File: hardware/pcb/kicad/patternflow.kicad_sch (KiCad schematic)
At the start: 35 parts, among them J1 Conn_02x08_Odd_Even, J2 Screw_Terminal_01x02, J3 Screw_Terminal_01x02, SW1 RotaryEncoder_Switch, SW2 RotaryEncoder_Switch, SW3 RotaryEncoder_Switch, SW4 RotaryEncoder_Switch, U1 ESP32-S3-DevKit-44pin

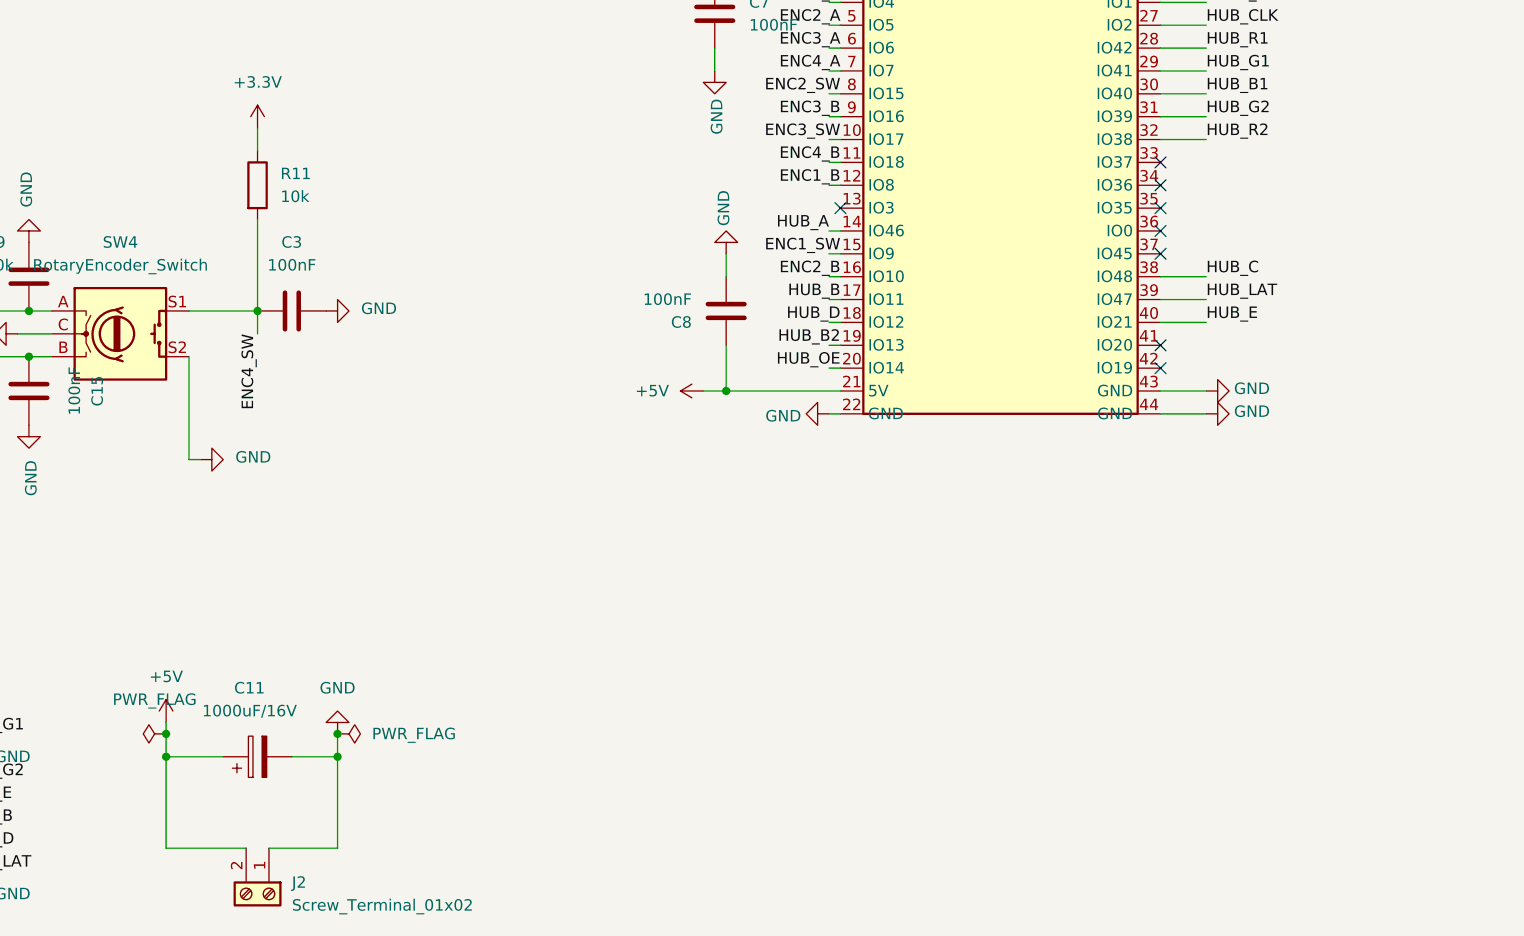
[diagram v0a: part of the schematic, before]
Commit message: GPIO0 pullup fix, encoder silkscreen fix
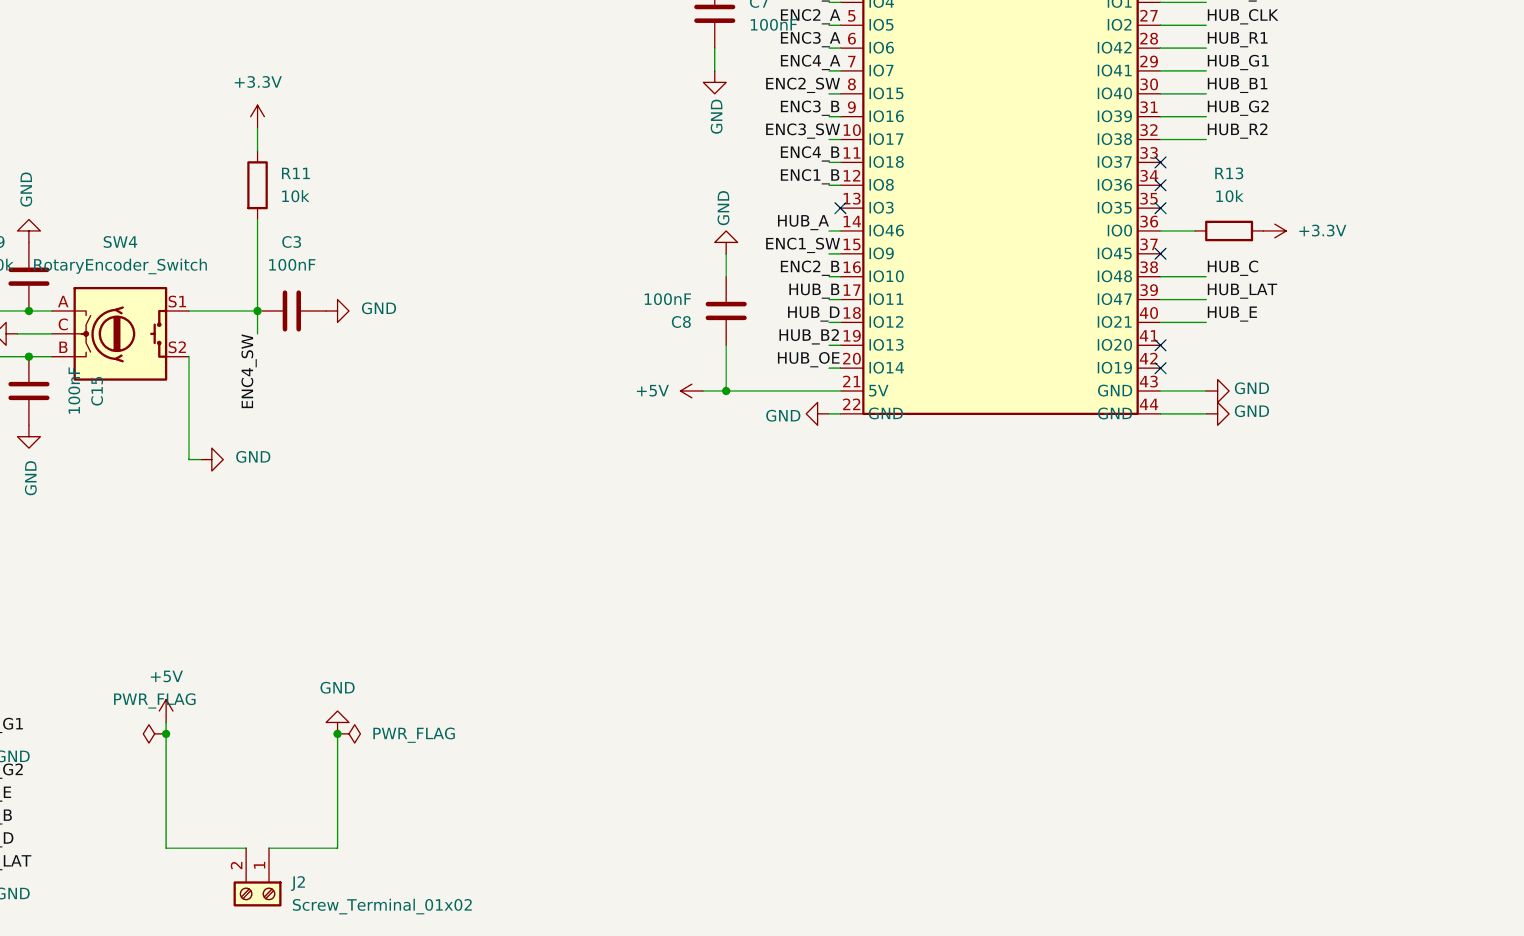
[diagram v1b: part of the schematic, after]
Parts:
- removed C11: 1000uF/16V, Capacitor_THT:CP_Radial_D10.0mm_P5.00mm, symbol Device:C_Polarized
- added R13: 10k, symbol Device:R
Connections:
- net +3.3V: now also R13.2
- net at U1.36 (IO0): now also R13.1
- no-connect marks 12 -> 11
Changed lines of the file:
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@@
 	)
 	(junction
-		(at 127 166.37)
-		(diameter 0)
-		(color 0 0 0 0)
-	)
-	(junction
 		(at 34.29 119.38)
 		(diameter 0)
@@
 	)
 	(junction
-		(at 146.05 166.37)
-		(diameter 0)
-		(color 0 0 0 0)
-	)
-	(junction
 		(at 127 163.83)
 		(diameter 0)
@@
 	)
 	(no_connect
-		(at 237.49 107.95)
-	)
-	(no_connect
 		(at 237.49 77.47)
 	)
@@
 	(wire
 		(pts
-			(xy 146.05 163.83) (xy 146.05 166.37)
+			(xy 146.05 163.83) (xy 146.05 176.53)
 		)
 		(stroke
@@
 	(wire
 		(pts
-			(xy 127 166.37) (xy 127 176.53)
+			(xy 127 163.83) (xy 127 176.53)
 		)
 		(stroke
@@
 	(wire
 		(pts
-			(xy 146.05 166.37) (xy 146.05 176.53)
-		)
-		(stroke
-			(width 0)
-			(type default)
-		)
-	)
-	(wire
-		(pts
 			(xy 200.66 118.11) (xy 201.93 118.11)
 		)
@@
 	(wire
 		(pts
-			(xy 140.97 166.37) (xy 146.05 166.37)
-		)
-		(stroke
-			(width 0)
-			(type default)
-		)
-	)
-	(wire
-		(pts
 			(xy 200.66 115.57) (xy 201.93 115.57)
 		)
@@
 	(wire
 		(pts
-			(xy 127 163.83) (xy 127 166.37)
+			(xy 104.14 66.04) (xy 113.03 66.04)
 		)
 		(stroke
@@
 	(wire
 		(pts
-			(xy 104.14 66.04) (xy 113.03 66.04)
+			(xy 129.54 66.04) (xy 129.54 77.47)
 		)
 		(stroke
@@
 	(wire
 		(pts
-			(xy 129.54 66.04) (xy 129.54 77.47)
+			(xy 137.16 50.8) (xy 137.16 60.96)
 		)
 		(stroke
@@
 	(wire
 		(pts
-			(xy 137.16 50.8) (xy 137.16 60.96)
+			(xy 237.49 107.95) (xy 241.3 107.95)
 		)
 		(stroke
@@
 		)
 	)
-	(wire
-		(pts
-			(xy 127 166.37) (xy 133.35 166.37)
-		)
-		(stroke
-			(width 0)
-			(type default)
-		)
-	)
 	(label "HUB_CLK"
 		(at 242.57 85.09 0)
@@
 	)
 	(symbol
+		(lib_id "Device:R")
+		(at 245.11 107.95 90)
+		(unit 1)
+		(body_style 1)
+		(exclude_from_sim no)
+		(in_bom yes)
+		(on_board yes)
+		(in_pos_files yes)
+		(dnp no)
+		(fields_autoplaced yes)
+		(property "Reference" "R13"
+			(at 245.11 101.6 90)
+			(show_name no)
+			(do_not_autoplace no)
+			(effects
+				(font
+					(size 1.27 1.27)
+				)
+			)
+		)
+		(property "Value" "10k"
+			(at 245.11 104.14 90)
+			(show_name no)
+			(do_not_autoplace no)
+			(effects
+				(font
+					(size 1.27 1.27)
+				)
+			)
+		)
+		(property "Footprint" ""
+			(at 245.11 109.728 90)
+			(hide yes)
+			(show_name no)
+			(do_not_autoplace no)
+			(effects
+				(font
+					(size 1.27 1.27)
+				)
+			)
+		)
+		(property "Datasheet" ""
+			(at 245.11 107.95 0)
+			(hide yes)
+			(show_name no)
+			(do_not_autoplace no)
+			(effects
+				(font
+					(size 1.27 1.27)
+				)
+			)
+		)
+		(property "Description" "Resistor"
+			(at 245.11 107.95 0)
+			(hide yes)
+			(show_name no)
+			(do_not_autoplace no)
+			(effects
+				(font
+					(size 1.27 1.27)
+				)
+			)
+		)
+		(pin "1"
+		)
+		(pin "2"
+		)
+		(instances
+			(project "patternflow"
+				(path "/7829ca74-397b-4e20-b2ed-d34479de16a0"
+					(reference "R13")
+					(unit 1)
+				)
+			)
+		)
+	)
+	(symbol
 		(lib_id "power:+5V")
 		(at 127 162.56 0)
@@
 	)
 	(symbol
+		(lib_id "power:+3.3V")
+		(at 248.92 107.95 270)
+		(unit 1)
+		(body_style 1)
+		(exclude_from_sim no)
+		(in_bom yes)
+		(on_board yes)
+		(in_pos_files yes)
+		(dnp no)
+		(fields_autoplaced yes)
+		(property "Reference" "#PWR03"
+			(at 245.11 107.95 0)
+			(hide yes)
+			(show_name no)
+			(do_not_autoplace no)
+			(effects
+				(font
+					(size 1.27 1.27)
+				)
+			)
+		)
+		(property "Value" "+3.3V"
+			(at 252.73 107.9499 90)
+			(show_name no)
+			(do_not_autoplace no)
+			(effects
+				(font
+					(size 1.27 1.27)
+				)
+				(justify left)
+			)
+		)
+		(property "Footprint" ""
+			(at 248.92 107.95 0)
+			(hide yes)
+			(show_name no)
+			(do_not_autoplace no)
+			(effects
+				(font
+					(size 1.27 1.27)
+				)
+			)
+		)
+		(property "Datasheet" ""
+			(at 248.92 107.95 0)
+			(hide yes)
+			(show_name no)
+			(do_not_autoplace no)
+			(effects
+				(font
+					(size 1.27 1.27)
+				)
+			)
+		)
+		(property "Description" "Power symbol creates a global label with name \"+3.3V\""
+			(at 248.92 107.95 0)
+			(hide yes)
+			(show_name no)
+			(do_not_autoplace no)
+			(effects
+				(font
+					(size 1.27 1.27)
+				)
+			)
+		)
+		(pin "1"
+		)
+		(instances
+			(project "patternflow"
+				(path "/7829ca74-397b-4e20-b2ed-d34479de16a0"
+					(reference "#PWR03")
+					(unit 1)
+				)
+			)
+		)
+	)
+	(symbol
 		(lib_id "power:GND")
 		(at 189.23 110.49 180)
@@
 					(unit 1)
 				)
-			)
-		)
-	)
-	(symbol
-		(lib_id "Device:C_Polarized")
-		(at 137.16 166.37 90)
-		(unit 1)
-		(body_style 1)
-		(exclude_from_sim no)
-		(in_bom yes)
-		(on_board yes)
-		(in_pos_files yes)
-		(dnp no)
-		(fields_autoplaced yes)
-		(property "Reference" "C11"
-			(at 136.271 158.75 90)
-			(show_name no)
-			(do_not_autoplace no)
-			(effects
-				(font
-					(size 1.27 1.27)
-				)
-			)
-		)
-		(property "Value" "1000uF/16V"
-			(at 136.271 161.29 90)
-			(show_name no)
-			(do_not_autoplace no)
-			(effects
-				(font
-					(size 1.27 1.27)
-				)
-			)
-		)
-		(property "Footprint" "Capacitor_THT:CP_Radial_D10.0mm_P5.00mm"
-			(at 140.97 165.4048 0)
-			(hide yes)
-			(show_name no)
-			(do_not_autoplace no)
-			(effects
-				(font
-					(size 1.27 1.27)
-				)
-			)
-		)
-		(property "Datasheet" ""
-			(at 137.16 166.37 0)
-			(hide yes)
-			(show_name no)
-			(do_not_autoplace no)
-			(effects
-				(font
-					(size 1.27 1.27)
-				)
-			)
-		)
-		(property "Description" "Polarized capacitor"
-			(at 137.16 166.37 0)
-			(hide yes)
-			(show_name no)
-			(do_not_autoplace no)
-			(effects
-				(font
-					(size 1.27 1.27)
-				)
-			)
-		)
-		(pin "1"
-		)
-		(pin "2"
-		)
-		(instances
-			(project "patternflow"
-				(path "/7829ca74-397b-4e20-b2ed-d34479de16a0"
-					(reference "C11")
-					(unit 1)
-				)
